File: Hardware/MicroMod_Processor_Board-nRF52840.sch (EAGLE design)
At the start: 25 parts, among them J2 MICROMOD-2222, U1 W25QXX128MBIT-6X5, U2 MDBT50Q, Y1 32.768kHz

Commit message: Routing
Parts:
- C1: device SparkFun-Capacitors:0.1UF-0402-16V-10% -> SparkFun-Capacitors:0.1UF-0402T-16V-10%
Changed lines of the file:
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@@
 <?xml version="1.0" encoding="utf-8"?>
 <!DOCTYPE eagle SYSTEM "eagle.dtd">
-<eagle version="9.5.2">
+<eagle version="9.4.2">
 <drawing>
 <settings>
-<setting alwaysvectorfont="no"/>
+<setting alwaysvectorfont="yes"/>
 <setting verticaltext="up"/>
 </settings>
@@
 <part name="LOGO2" library="SparkFun-Aesthetics" deviceset="SFE_LOGO_FLAME" device=".1_INCH"/>
 <part name="U1" library="SparkFun-MicroMod" deviceset="W25QXX" device="128MBIT-6X5"/>
-<part name="C1" library="SparkFun-Capacitors" deviceset="0.1UF" device="-0402-16V-10%" value="0.1uF"/>
+<part name="C1" library="SparkFun-Capacitors" deviceset="0.1UF" device="-0402T-16V-10%" value="0.1uF"/>
 <part name="SUPPLY2" library="SparkFun-PowerSymbols" deviceset="3.3V" device=""/>
 <part name="GND2" library="SparkFun-PowerSymbols" deviceset="GND" device=""/>

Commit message: Routing
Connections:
- net ADC_D+: now also U2.P0.29(AIN5); no longer U2.P0.28(AIN4)
- net ADC_D-: now also U2.P0.03(AIN1); no longer U2.P0.02(AIN0)
- net BATT_VIN/3: now also U2.P0.30(AIN6); no longer U2.P0.29(AIN5)
- net CTS1: now also U2.P1.09(TRACEDATA3); no longer U2.P0.06
- net PWM0: now also U2.P0.06; no longer U2.P1.09(TRACEDATA3)
- net SPI_MISO1: now also U2.P0.02(AIN0); no longer U2.P0.31(AIN7)
- net SPI_MOSI1: now also U2.P0.31(AIN7); no longer U2.P0.03(AIN1)
- net SPI_SCK1: now also U2.P0.28(AIN4); no longer U2.P0.30(AIN6)

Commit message: Routing
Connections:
- net RX1: now also U2.P0.17; no longer U2.P0.15
- net TX1: now also U2.P0.15; no longer U2.P0.17
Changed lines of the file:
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@@
 <?xml version="1.0" encoding="utf-8"?>
 <!DOCTYPE eagle SYSTEM "eagle.dtd">
-<eagle version="9.5.2">
+<eagle version="9.4.2">
 <drawing>
 <settings>
-<setting alwaysvectorfont="no"/>
+<setting alwaysvectorfont="yes"/>
 <setting verticaltext="up"/>
 </settings>
-<grid distance="0.05" unitdist="inch" unit="inch" style="lines" multiple="1" display="yes" altdistance="0.005" altunitdist="inch" altunit="inch"/>
+<grid distance="0.1" unitdist="inch" unit="inch" style="lines" multiple="1" display="no" altdistance="0.01" altunitdist="inch" altunit="inch"/>
 <layers>
 <layer number="1" name="Top" color="4" fill="1" visible="no" active="no"/>
@@
 </segment>
 <segment>
+<pinref part="U2" gate="G$1" pin="P0.15"/>
+<wire x1="210.82" y1="213.36" x2="213.36" y2="213.36" width="0.1524" layer="91"/>
+<label x="213.36" y="213.36" size="1.27" layer="95" xref="yes"/>
+</segment>
+</net>
+<net name="RX1" class="0">
+<segment>
+<wire x1="76.2" y1="203.2" x2="78.74" y2="203.2" width="0.1524" layer="91"/>
+<label x="78.74" y="203.2" size="1.27" layer="95" xref="yes"/>
+<pinref part="J2" gate="J1" pin="RX1"/>
+</segment>
+<segment>
 <pinref part="U2" gate="G$1" pin="P0.17"/>
 <wire x1="210.82" y1="208.28" x2="213.36" y2="208.28" width="0.1524" layer="91"/>
@@
 </segment>
 </net>
-<net name="RX1" class="0">
-<segment>
-<wire x1="76.2" y1="203.2" x2="78.74" y2="203.2" width="0.1524" layer="91"/>
-<label x="78.74" y="203.2" size="1.27" layer="95" xref="yes"/>
-<pinref part="J2" gate="J1" pin="RX1"/>
-</segment>
-<segment>
-<pinref part="U2" gate="G$1" pin="P0.15"/>
-<wire x1="210.82" y1="213.36" x2="213.36" y2="213.36" width="0.1524" layer="91"/>
-<label x="213.36" y="213.36" size="1.27" layer="95" xref="yes"/>
-</segment>
-</net>

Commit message: Placed silk screen
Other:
- note added: "USB_VIN = -0.3 to +5.8V"
- note added: "VDD = -0.3 to +3.9V"
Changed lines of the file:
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@@
 <text x="421.64" y="7.62" size="2.54" layer="94">v1.0</text>
 <text x="53.34" y="60.96" size="2.54" layer="94" align="center">128Mb Flash</text>
+<text x="33.02" y="144.78" size="2.54" layer="96">USB_VIN = -0.3 to +5.8V</text>
+<text x="172.72" y="147.32" size="2.54" layer="96">VDD = -0.3 to +3.9V</text>
 </plain>
 <instances>

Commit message: Implemented changes from first design review
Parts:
- R2, R3: value 27 -> 27OHM; device SparkFun-Resistors:27OHM-0603-1/10W-1% -> SparkFun-Resistors:27OHM
- renumbered D2 to D1, J2 to J1
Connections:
- net USB_VIN renamed V_USB
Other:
- note added: "Voltage Range: 1.7 to 5.5V"
- note added: "Voltage Range: 4.45 to 5.25V"
- note added: "nRF52840"
- note added: "v01"
- note removed: "0.65uA Leakage 0.3V drop at 10mA"
- note removed: "USB_VIN = -0.3 to +5.8V"
- note removed: "VDD = -0.3 to +3.9V"
- note removed: "v1.0"
- moved on the sheet: C2, C3, Y1

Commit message: Going over check list
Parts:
- U2: device nrf52840:MDBT50Q -> SparkFun-RF:MDBT50Q

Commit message: Changes from QC Double Check
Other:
- note removed: "Voltage Range: 4.45 to 5.25V"
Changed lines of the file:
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@@
 <text x="424.434" y="8.382" size="2.54" layer="94" font="vector" align="center">v01</text>
 <text x="53.34" y="60.96" size="2.54" layer="94" font="vector" align="center">128Mb Flash</text>
-<text x="51.054" y="146.05" size="2.54" layer="96" font="vector" align="center">Voltage Range: 4.45 to 5.25V</text>
 <text x="190.5" y="147.828" size="2.54" layer="96" font="vector" align="center">Voltage Range: 1.7 to 5.5V</text>
 <text x="190.754" y="268.986" size="2.54" layer="94" font="vector" align="center">nRF52840</text>
@@
 </instance>
 <instance part="R2" gate="G$1" x="157.48" y="238.76" smashed="yes">
-<attribute name="NAME" x="154.94" y="240.284" size="1.778" layer="95" font="vector" align="bottom-center"/>
+<attribute name="NAME" x="152.4" y="240.284" size="1.778" layer="95" font="vector" align="bottom-center"/>
+<attribute name="VALUE" x="162.56" y="242.316" size="1.778" layer="96" font="vector" align="top-center"/>
 </instance>
 <instance part="R3" gate="G$1" x="157.48" y="236.22" smashed="yes">
-<attribute name="NAME" x="154.94" y="232.664" size="1.778" layer="95" font="vector" align="bottom-center"/>
+<attribute name="NAME" x="152.4" y="232.664" size="1.778" layer="95" font="vector" align="bottom-center"/>
+<attribute name="VALUE" x="162.56" y="234.696" size="1.778" layer="96" font="vector" align="top-center"/>
 </instance>
 <instance part="SUPPLY3" gate="G$1" x="162.56" y="256.54" smashed="yes">

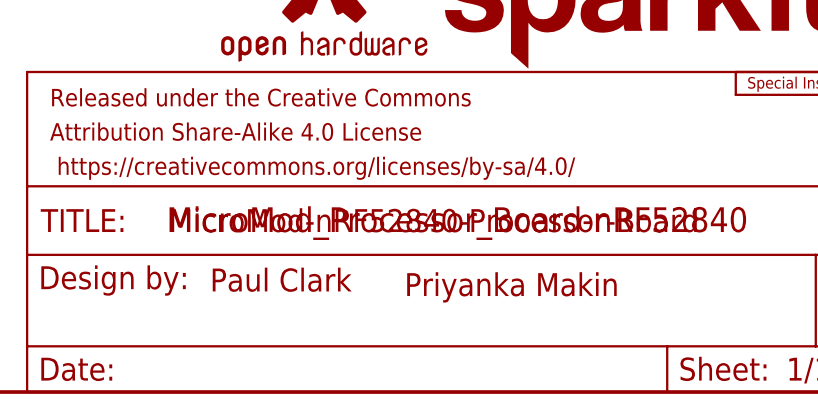
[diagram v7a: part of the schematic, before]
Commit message: Added more GND vias and made top polygon isolate larger
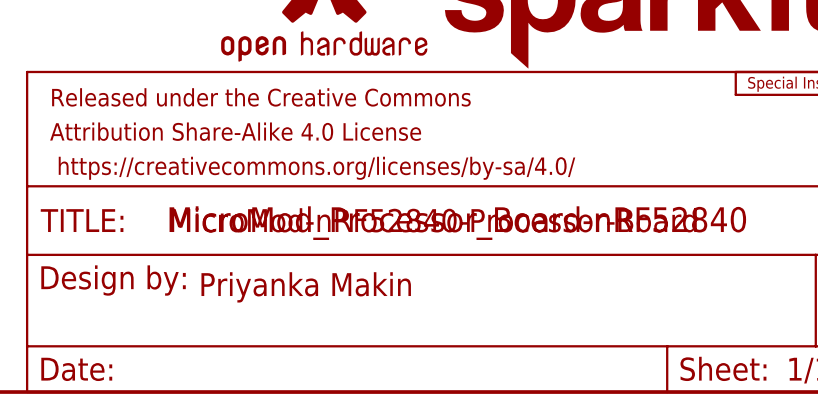
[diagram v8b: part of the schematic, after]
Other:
- note removed: "Paul Clark"
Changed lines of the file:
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@@
 <?xml version="1.0" encoding="utf-8"?>
 <!DOCTYPE eagle SYSTEM "eagle.dtd">
-<eagle version="9.5.2">
+<eagle version="9.4.2">
 <drawing>
 <settings>
-<setting alwaysvectorfont="no"/>
+<setting alwaysvectorfont="yes"/>
 <setting verticaltext="up"/>
 </settings>
@@
 <text x="56.134" y="124.206" size="2.54" layer="94" font="vector" align="center">Status LED</text>
 <text x="375.412" y="19.05" size="2.54" layer="94" font="vector" align="center">MicroMod-nRF52840-Processor-Board</text>
-<text x="358.394" y="12.446" size="2.54" layer="94" font="vector" align="center">Paul Clark</text>
-<text x="384.048" y="11.938" size="2.54" layer="94" font="vector" align="center">Priyanka Makin</text>
+<text x="361.188" y="11.938" size="2.54" layer="94" font="vector" align="center">Priyanka Makin</text>
 <text x="424.434" y="8.382" size="2.54" layer="94" font="vector" align="center">v01</text>
 <text x="53.34" y="60.96" size="2.54" layer="94" font="vector" align="center">128Mb Flash</text>
